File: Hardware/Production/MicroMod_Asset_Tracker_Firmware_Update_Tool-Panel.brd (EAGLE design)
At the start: 199.6 x 83.1 mm, 582 parts, among them J12 MICROMOD-2222, J15 MICROMOD-2222, J18 MICROMOD-2222, J21 MICROMOD-2222, J24 MICROMOD-2222, J27 MICROMOD-2222, J30 MICROMOD-2222, J33 MICROMOD-2222, J36 MICROMOD-2222, J39 MICROMOD-2222, J42 MICROMOD-2222, J45 MICROMOD-2222, J48 MICROMOD-2222, J5 MICROMOD-2222, J6 MICROMOD-2222, J9 MICROMOD-2222, U1 CH340G, U10 CH340G, U11 CH340G, U12 CH340G, U13 CH340G, U14 CH340G, U15 CH340G, U16 CH340G, U2 CH340G, U3 CH340G, U4 CH340G, U5 CH340G, U6 CH340G, U7 CH340G, U8 CH340G, U9 CH340G, Y1 12MHz, Y10 12MHz, Y11 12MHz, Y12 12MHz, Y13 12MHz, Y14 12MHz, Y15 12MHz, Y16 12MHz, Y2 12MHz, Y3 12MHz, Y4 12MHz, Y5 12MHz, Y6 12MHz, Y7 12MHz, Y8 12MHz, Y9 12MHz

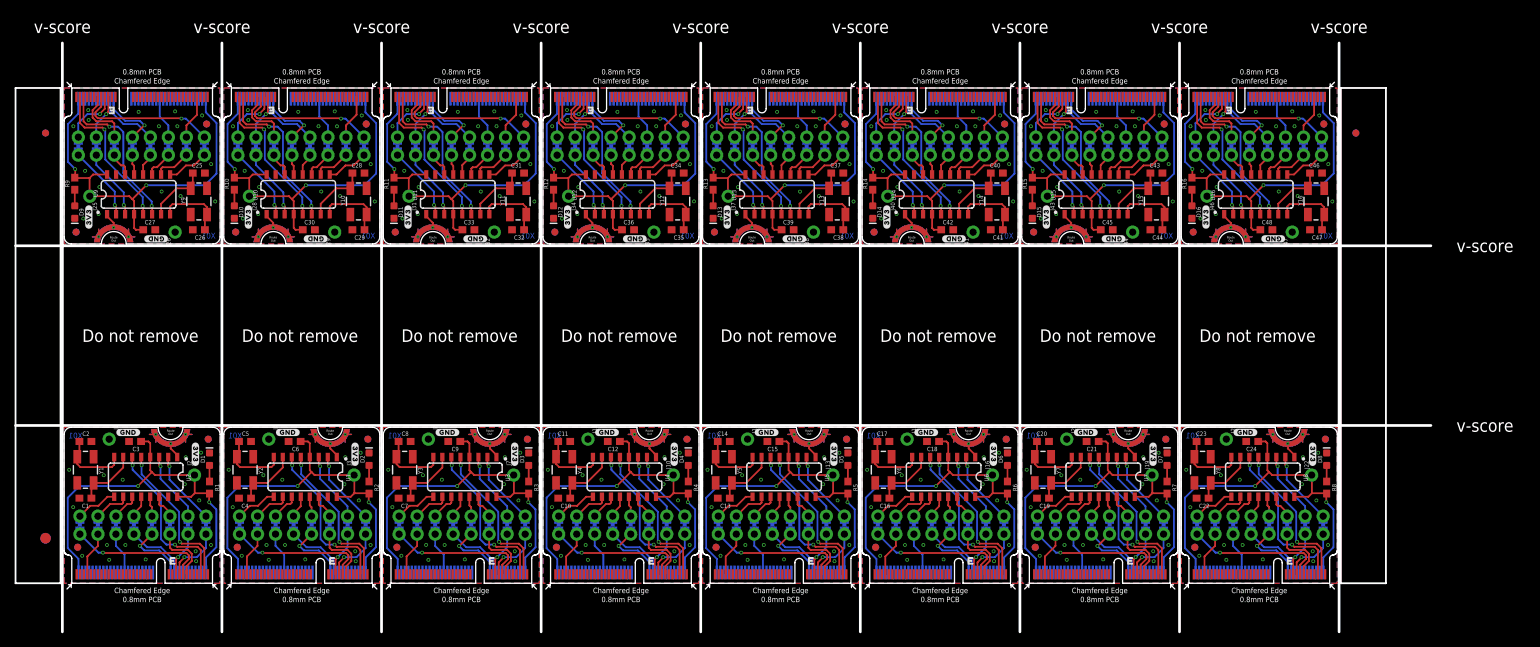
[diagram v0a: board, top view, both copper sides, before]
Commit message: Changed to the CH340C
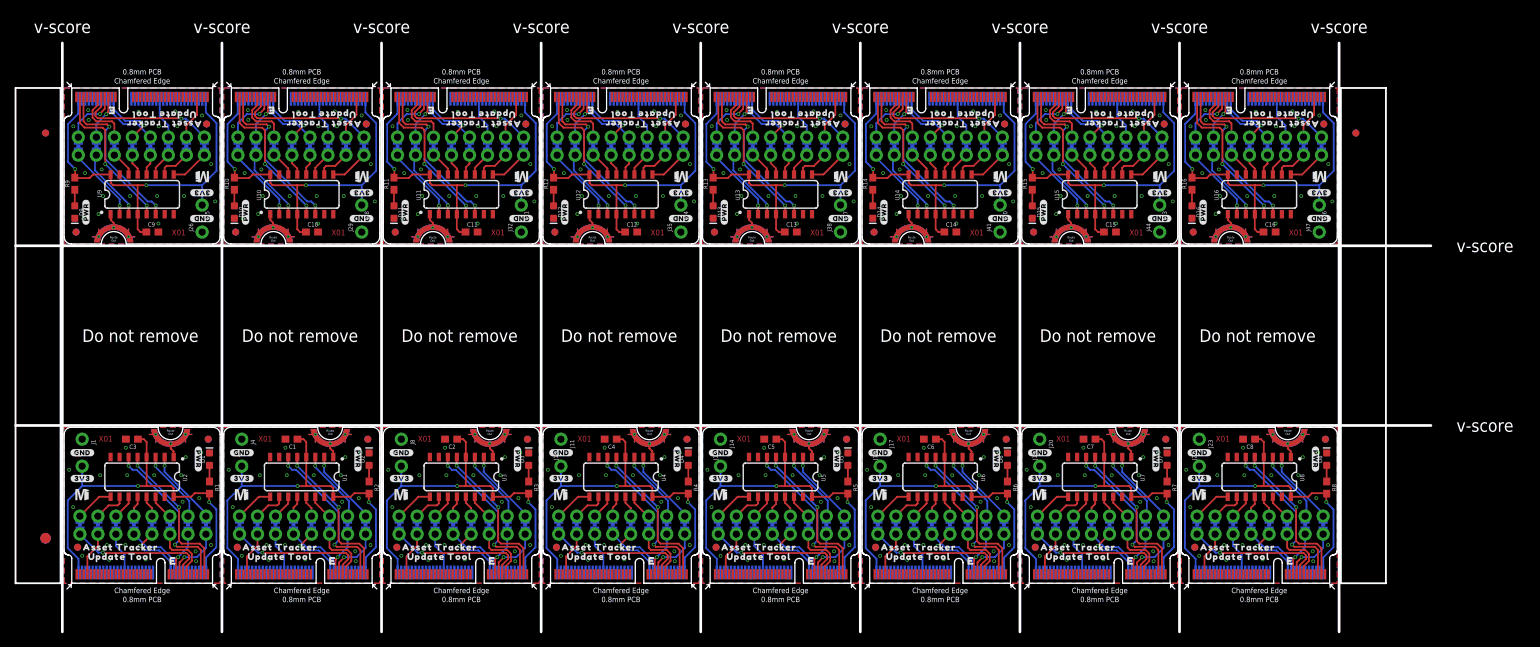
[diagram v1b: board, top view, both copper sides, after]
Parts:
- removed C17, C19, C20, C22, C23, C25, C26, C28, C29, C31, C32, C34, C35, C37, C38, C40, C41, C43, C44, C46, C47: 18pF, SparkFun-Capacitors:0603
- removed C18, C21, C24, C27, C30, C33, C36, C39, C42, C45, C48: 0.1uF, SparkFun-Capacitors:0603
- removed Y1, Y10, Y11, Y12, Y13, Y14, Y15, Y16, Y2, Y3, Y4, Y5, Y6, Y7, Y8, Y9: 12MHz, SparkFun-Clocks:CRYSTAL-SMD-5X3.2-4PAD
- added U$193, U$204, U$209, U$220, U$225, U$236, U$241, U$252: (no value), output:#GND#2
- added U$194, U$203, U$210, U$219, U$226, U$235, U$242, U$251: (no value), output:#3V3#3
- added U$195, U$211, U$227, U$243: (no value), output:#CTS#0
- added U$196, U$212, U$228, U$244: (no value), output:#DSR#0
- added U$197, U$213, U$229, U$245: (no value), output:#RTS#0
- added U$198, U$214, U$230, U$246: (no value), output:#DCD#0
- added U$199, U$215, U$231, U$247: (no value), output:#TX#0
- added U$200, U$216, U$232, U$248: (no value), output:#RX#0
- added U$201, U$217, U$233, U$249: (no value), output:#DTR#0
- added U$202, U$218, U$234, U$250: (no value), output:#RI#0
- added U$205, U$221, U$237, U$253: (no value), output:#PWR#0
- added U$206, U$222, U$238, U$254: (no value), SparkFun-MicroMod:MICROMOD_MI_LOGO_.35
- added U$207, U$223, U$239, U$255: (no value), output:ASSET_TRACKER0
- added U$208, U$224, U$240, U$256: (no value), output:UPDATE_TOOL0
- C1, C10, C11, C13, C14, C16, C2, C4, C5, C7, C8: value 18pF -> 0.1uF
- U$10, U$111, U$159, U$63: device output:#CTS#0 -> output:ASSET_TRACKER0
- U$109, U$157, U$61, U$8: device output:#GND#2 -> output:#PWR#0
- U$11, U$112, U$160, U$64: device output:#DSR#0 -> output:UPDATE_TOOL0
- U$110, U$158, U$62, U$9: device output:#3V3#3 -> SparkFun-MicroMod:MICROMOD_MI_LOGO_.35
- U$113, U$12, U$161, U$65: device output:#RTS#0 -> output:#GND#2
- U$114, U$13, U$162, U$66: device output:#DCD#0 -> output:#3V3#3
- U$115, U$15, U$163, U$67: device output:#TX#0 -> output:#CTS#0
- U$116, U$16, U$164, U$68: device output:#RX#0 -> output:#DSR#0
- U$117, U$165, U$19, U$69: device output:#DTR#0 -> output:#RTS#0
- U$118, U$166, U$21, U$70: device output:#RI#0 -> output:#DCD#0
- U$119, U$167, U$22, U$71: device output:#3V3#3 -> output:#TX#0
- U$120, U$168, U$24, U$72: device output:#GND#2 -> output:#RX#0
- U$121, U$169, U$25, U$73: device output:#GND#2 -> output:#DTR#0
- U$122, U$170, U$26, U$74: device output:#3V3#3 -> output:#RI#0
- U$123, U$171, U$27, U$75: device output:#CTS#0 -> output:#3V3#3
- U$124, U$172, U$28, U$76: device output:#DSR#0 -> output:#GND#2
- U$125, U$173, U$29, U$77: device output:#RTS#0 -> output:#PWR#0
- U$126, U$174, U$30, U$78: device output:#DCD#0 -> SparkFun-MicroMod:MICROMOD_MI_LOGO_.35
- U$127, U$175, U$31, U$79: device output:#TX#0 -> output:ASSET_TRACKER0
- U$128, U$176, U$32, U$80: device output:#RX#0 -> output:UPDATE_TOOL0
- U$129, U$177, U$33, U$81: device output:#DTR#0 -> output:#GND#2
- U$130, U$178, U$34, U$82: device output:#RI#0 -> output:#3V3#3
- U$131, U$179, U$35, U$83: device output:#3V3#3 -> output:#CTS#0
- U$132, U$180, U$36, U$84: device output:#GND#2 -> output:#DSR#0
- U$133, U$181, U$37, U$85: device output:#GND#2 -> output:#RTS#0
- U$134, U$182, U$38, U$86: device output:#3V3#3 -> output:#DCD#0
- U$135, U$183, U$39, U$87: device output:#CTS#0 -> output:#TX#0
- U$136, U$184, U$40, U$88: device output:#DSR#0 -> output:#RX#0
- U$137, U$185, U$41, U$89: device output:#RTS#0 -> output:#DTR#0
- U$138, U$186, U$42, U$90: device output:#DCD#0 -> output:#RI#0
- U$139, U$187, U$43, U$91: device output:#TX#0 -> output:#3V3#3
- U$140, U$188, U$44, U$92: device output:#RX#0 -> output:#GND#2
- U$141, U$189, U$45, U$93: device output:#DTR#0 -> output:#PWR#0
- U$142, U$190, U$46, U$94: device output:#RI#0 -> SparkFun-MicroMod:MICROMOD_MI_LOGO_.35
- U$143, U$191, U$47, U$95: device output:#3V3#3 -> output:ASSET_TRACKER0
- U$144, U$192, U$48, U$96: device output:#GND#2 -> output:UPDATE_TOOL0
- U1, U10, U11, U12, U13, U14, U15, U16, U2, U3, U4, U5, U6, U7, U8, U9: value CH340G -> CH340C
- moved U$103 159.6 mm to (155.1, 12.3), turned to 90 degrees
- moved U$119 156.6 mm to (177.6, 12.3), turned to 90 degrees
- moved U$104 154.8 mm to (152.5, 12.3), turned to 90 degrees
- moved U$101 149.7 mm to (149.9, 12.5), turned to 90 degrees
- moved U$117 147.3 mm to (172.4, 12.5), turned to 90 degrees
- moved U$105 144.9 mm to (147.4, 12.5), turned to 90 degrees
- moved U$120 144.2 mm to (175.0, 12.3), turned to 90 degrees
- moved U$116 142.6 mm to (162.3, 12.4), turned to 90 degrees
- moved U$115 142.6 mm to (159.8, 12.5), turned to 90 degrees
- moved U$102 140.1 mm to (144.9, 12.5), turned to 90 degrees
- moved U$98 139.1 mm to (137.6, 14.8), turned to 0 degrees
- moved U$107 139.1 mm to (137.6, 14.8), turned to 0 degrees
- moved U$118 137.9 mm to (167.4, 12.5), turned to 90 degrees
- moved U$113 136.2 mm to (160.1, 18.4), flipped to the top, turned to 0 degrees
- moved U$106 135.7 mm to (142.4, 11.9), turned to 90 degrees
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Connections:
- removed net N$1 (its old number): C2.2, U2.8, Y1.1
- removed net N$10 (its old number): C10.2, U4.7, Y4.3
- removed net N$11 (its old number): C11.2, U4.8, Y4.1
- removed net N$13 (its old number): C13.2, U5.7, Y5.3
- removed net N$14 (its old number): C14.2, U5.8, Y5.1
- removed net N$16 (its old number): C16.2, U6.7, Y6.3
- removed net N$17: C17.2, U6.8, Y6.1
- removed net N$19: C19.2, U7.7, Y7.3
- removed net N$2 (its old number): C1.2, U2.7, Y1.3
- removed net N$20: C20.2, U7.8, Y7.1
- removed net N$22: C22.2, U8.7, Y8.3
- removed net N$23: C23.2, U8.8, Y8.1
- removed net N$25: C25.2, U9.7, Y9.3
- removed net N$26: C26.2, U9.8, Y9.1
- removed net N$28: C28.2, U10.7, Y10.3
- removed net N$29: C29.2, U10.8, Y10.1
- removed net N$31: C31.2, U11.7, Y11.3
- removed net N$32: C32.2, U11.8, Y11.1
- removed net N$34: C34.2, U12.7, Y12.3
- removed net N$35: C35.2, U12.8, Y12.1
- removed net N$37: C37.2, U13.7, Y13.3
- removed net N$38: C38.2, U13.8, Y13.1
- removed net N$4 (its old number): C4.2, U1.7, Y2.3
- removed net N$40: C40.2, U14.7, Y14.3
- removed net N$41: C41.2, U14.8, Y14.1
- removed net N$43: C43.2, U15.7, Y15.3
- removed net N$44: C44.2, U15.8, Y15.1
- removed net N$46: C46.2, U16.7, Y16.3
- removed net N$47: C47.2, U16.8, Y16.1
- removed net N$5 (its old number): C5.2, U1.8, Y2.1
- removed net N$7 (its old number): C7.2, U3.7, Y3.3
- removed net N$8 (its old number): C8.2, U3.8, Y3.1
- net 3.3V1: now also C1.1; no longer C6.1
- net 3.3V10: now also C11.1; no longer C33.1
- net 3.3V11: now also C12.1; no longer C36.1
- net 3.3V12: now also C13.1; no longer C39.1
- net 3.3V13: now also C14.1; no longer C42.1
- net 3.3V14: now also C15.1; no longer C45.1
- net 3.3V15: now also C16.1; no longer C48.1
- net 3.3V2: now also C2.1; no longer C9.1
- net 3.3V3: now also C4.1; no longer C12.1
- net 3.3V4: now also C5.1; no longer C15.1
- net 3.3V5: now also C6.1; no longer C18.1
- net 3.3V6: now also C7.1; no longer C21.1
- net 3.3V7: now also C8.1; no longer C24.1
- net 3.3V8: now also C9.1; no longer C27.1
- net 3.3V9: now also C10.1; no longer C30.1
- net GND: no longer C1.1, C2.1
- net GND1: now also C1.2; no longer C4.1, C5.1, C6.2
- net GND10: now also C11.2; no longer C31.1, C32.1, C33.2
- net GND11: now also C12.2; no longer C34.1, C35.1, C36.2
- net GND12: now also C13.2; no longer C37.1, C38.1, C39.2
- net GND13: now also C14.2; no longer C40.1, C41.1, C42.2
- net GND14: now also C15.2; no longer C43.1, C44.1, C45.2
- net GND15: now also C16.2; no longer C46.1, C47.1, C48.2
- net GND2: now also C2.2; no longer C7.1, C8.1, C9.2
- net GND3: now also C4.2; no longer C10.1, C11.1, C12.2
- net GND4: now also C5.2; no longer C13.1, C14.1, C15.2
- net GND5: now also C6.2; no longer C16.1, C17.1, C18.2
- net GND6: now also C7.2; no longer C19.1, C20.1, C21.2
- net GND7: now also C8.2; no longer C22.1, C23.1, C24.2
- net GND8: now also C9.2; no longer C25.1, C26.1, C27.2
- net GND9: now also C10.2; no longer C28.1, C29.1, C30.2
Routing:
- net N$47: track 9.92 -> 0.00 mm
- net N$44: track 9.92 -> 0.00 mm
- net N$29: track 9.92 -> 0.00 mm
- net N$26: track 9.92 -> 0.00 mm
- net N$1 (its old number): track 9.92 -> 0.00 mm
- net N$5 (its old number): track 9.92 -> 0.00 mm
- net N$11 (its old number): track 9.92 -> 0.00 mm
- net N$8 (its old number): track 9.92 -> 0.00 mm
- net N$17: track 9.92 -> 0.00 mm
- net N$14 (its old number): track 9.92 -> 0.00 mm
- net N$38: track 9.92 -> 0.00 mm
- net N$35: track 9.92 -> 0.00 mm
- net N$32: track 9.92 -> 0.00 mm
- net N$23: track 9.92 -> 0.00 mm
- net N$20: track 9.92 -> 0.00 mm
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
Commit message: Updates for v10
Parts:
- removed SPARKX1, SPARKX10, SPARKX11, SPARKX12, SPARKX13, SPARKX14, SPARKX15, SPARKX16, SPARKX2, SPARKX3, SPARKX4, SPARKX5, SPARKX6, SPARKX7, SPARKX8, SPARKX9: SPARKX-LOGO4, SparkX:SPARKX-MEDIUM
- added LOGO17, LOGO19, LOGO21, LOGO23, LOGO25, LOGO27, LOGO29, LOGO31: OSHW-LOGOMINI, SparkFun-Aesthetics:OSHW-LOGO-MINI
- added LOGO18, LOGO20, LOGO22, LOGO24, LOGO26, LOGO28, LOGO30, LOGO32: SFE_LOGO_NAME_FLAME.1_INCH, SparkFun-Aesthetics:SFE_LOGO_NAME_FLAME_.1
- added U$257, U$266: (no value), output:#3V3#3
- added U$258: (no value), output:#CTS#0
- added U$259: (no value), output:#DSR#0
- added U$260: (no value), output:#RTS#0
- added U$261: (no value), output:#DCD#0
- added U$262: (no value), output:#TX#0
- added U$263: (no value), output:#RX#0
- added U$264: (no value), output:#DTR#0
- added U$265: (no value), output:#RI#0
- added U$267: (no value), output:#GND#2
- added U$268: (no value), output:#PWR#0
- added U$269: (no value), SparkFun-MicroMod:MICROMOD_MI_LOGO_.35
- added U$270: (no value), output:ASSET_TRACKER0
- added U$271: (no value), output:UPDATE_TOOL0
- added U$272: (no value), SparkFun-MicroMod:MICROMOD_LOGO_.35
- LOGO10, LOGO12, LOGO14, LOGO16, LOGO3, LOGO4, LOGO6, LOGO8: value OSHW-LOGOMINI -> SFE_LOGO_NAME_FLAME.1_INCH; device SparkFun-Aesthetics:OSHW-LOGO-MINI -> SparkFun-Aesthetics:SFE_LOGO_NAME_FLAME_.1
- U$100: device output:#DSR#0 -> output:ASSET_TRACKER0
- U$101: device output:#RTS#0 -> output:UPDATE_TOOL0
- U$102: device output:#DCD#0 -> SparkFun-MicroMod:MICROMOD_LOGO_.35
- U$103, U$199: device output:#TX#0 -> output:#GND#2
- U$104, U$232: device output:#RX#0 -> output:#3V3#3
- U$105: device output:#DTR#0 -> output:#CTS#0
- U$106: device output:#RI#0 -> output:#DSR#0
- U$107, U$226: device output:#3V3#3 -> output:#RTS#0
- U$108, U$193: device output:#GND#2 -> output:#DCD#0
- U$109: device output:#PWR#0 -> output:#TX#0
- U$110: device SparkFun-MicroMod:MICROMOD_MI_LOGO_.35 -> output:#RX#0
- U$111: device output:ASSET_TRACKER0 -> output:#DTR#0
- U$112: device output:UPDATE_TOOL0 -> output:#RI#0
- U$113, U$172, U$28: device output:#GND#2 -> output:#3V3#3
- U$114, U$13, U$171: device output:#3V3#3 -> output:#GND#2
- U$115: device output:#CTS#0 -> output:#PWR#0
- U$116: device output:#DSR#0 -> SparkFun-MicroMod:MICROMOD_MI_LOGO_.35
- U$117: device output:#RTS#0 -> output:ASSET_TRACKER0
- U$118: device output:#DCD#0 -> output:UPDATE_TOOL0
- U$119: device output:#TX#0 -> SparkFun-MicroMod:MICROMOD_LOGO_.35
- U$12, U$204: device output:#GND#2 -> SparkFun-MicroMod:MICROMOD_LOGO_.35
- U$120, U$216: device output:#RX#0 -> output:#GND#2
- U$121, U$249: device output:#DTR#0 -> output:#3V3#3
- U$122: device output:#RI#0 -> output:#CTS#0
- U$123, U$242: device output:#3V3#3 -> output:#DSR#0
- U$124, U$209: device output:#GND#2 -> output:#RTS#0
- U$125: device output:#PWR#0 -> output:#DCD#0
- U$126: device SparkFun-MicroMod:MICROMOD_MI_LOGO_.35 -> output:#TX#0
- U$127: device output:ASSET_TRACKER0 -> output:#RX#0
- U$128: device output:UPDATE_TOOL0 -> output:#DTR#0
- U$129, U$44: device output:#GND#2 -> output:#RI#0
- U$131, U$35: device output:#CTS#0 -> output:#GND#2
- U$132: device output:#DSR#0 -> output:#PWR#0
- U$133: device output:#RTS#0 -> SparkFun-MicroMod:MICROMOD_MI_LOGO_.35
- U$134: device output:#DCD#0 -> output:ASSET_TRACKER0
- U$135: device output:#TX#0 -> output:UPDATE_TOOL0
- U$136: device output:#RX#0 -> SparkFun-MicroMod:MICROMOD_LOGO_.35
- U$137, U$233: device output:#DTR#0 -> output:#GND#2
- U$138: device output:#RI#0 -> output:#3V3#3
- U$139: device output:#3V3#3 -> output:#CTS#0
- U$140, U$225: device output:#GND#2 -> output:#DSR#0
- U$141: device output:#PWR#0 -> output:#RTS#0
- U$142: device SparkFun-MicroMod:MICROMOD_MI_LOGO_.35 -> output:#DCD#0
- U$143: device output:ASSET_TRACKER0 -> output:#TX#0
- U$144: device output:UPDATE_TOOL0 -> output:#RX#0
- U$145, U$60: device output:#GND#2 -> output:#DTR#0
- U$146, U$27: device output:#3V3#3 -> output:#RI#0
- U$147, U$15: device output:#CTS#0 -> output:#3V3#3
- U$148, U$52: device output:#DSR#0 -> output:#GND#2
- U$149: device output:#RTS#0 -> output:#PWR#0
- U$150: device output:#DCD#0 -> SparkFun-MicroMod:MICROMOD_MI_LOGO_.35
- U$151: device output:#TX#0 -> output:ASSET_TRACKER0
- U$152: device output:#RX#0 -> output:UPDATE_TOOL0
- U$153: device output:#DTR#0 -> SparkFun-MicroMod:MICROMOD_LOGO_.35
- U$154, U$250: device output:#RI#0 -> output:#GND#2
- U$156, U$241: device output:#GND#2 -> output:#CTS#0
- U$157: device output:#PWR#0 -> output:#DSR#0
- U$158: device SparkFun-MicroMod:MICROMOD_MI_LOGO_.35 -> output:#RTS#0
- U$159: device output:ASSET_TRACKER0 -> output:#DCD#0
- U$16: device output:#DSR#0 -> output:#CTS#0
- U$160: device output:UPDATE_TOOL0 -> output:#TX#0
- U$161, U$76: device output:#GND#2 -> output:#RX#0
- U$162, U$43: device output:#3V3#3 -> output:#DTR#0
- U$163: device output:#CTS#0 -> output:#RI#0
- U$164, U$36: device output:#DSR#0 -> output:#3V3#3
- U$165, U$69: device output:#RTS#0 -> output:#GND#2
- U$166: device output:#DCD#0 -> output:#PWR#0
- U$167: device output:#TX#0 -> SparkFun-MicroMod:MICROMOD_MI_LOGO_.35
- U$168: device output:#RX#0 -> output:ASSET_TRACKER0
- U$169: device output:#DTR#0 -> output:UPDATE_TOOL0
- U$170: device output:#RI#0 -> SparkFun-MicroMod:MICROMOD_LOGO_.35
- U$173: device output:#PWR#0 -> output:#CTS#0
- U$174: device SparkFun-MicroMod:MICROMOD_MI_LOGO_.35 -> output:#DSR#0
- U$175: device output:ASSET_TRACKER0 -> output:#RTS#0
- U$176: device output:UPDATE_TOOL0 -> output:#DCD#0
- U$177, U$92: device output:#GND#2 -> output:#TX#0
- U$178, U$59: device output:#3V3#3 -> output:#RX#0
- U$179: device output:#CTS#0 -> output:#DTR#0
- U$180: device output:#DSR#0 -> output:#RI#0
- U$181, U$53: device output:#RTS#0 -> output:#3V3#3
- U$182, U$86: device output:#DCD#0 -> output:#GND#2
- U$183: device output:#TX#0 -> output:#PWR#0
- U$184: device output:#RX#0 -> SparkFun-MicroMod:MICROMOD_MI_LOGO_.35
- U$185: device output:#DTR#0 -> output:ASSET_TRACKER0
- U$186: device output:#RI#0 -> output:UPDATE_TOOL0
- U$187, U$34: device output:#3V3#3 -> SparkFun-MicroMod:MICROMOD_LOGO_.35
- U$189, U$45: device output:#PWR#0 -> output:#3V3#3
- U$19: device output:#RTS#0 -> output:#DSR#0
- U$190: device SparkFun-MicroMod:MICROMOD_MI_LOGO_.35 -> output:#CTS#0
- U$191: device output:ASSET_TRACKER0 -> output:#DSR#0
- U$192: device output:UPDATE_TOOL0 -> output:#RTS#0
- U$194, U$75: device output:#3V3#3 -> output:#TX#0
- U$195: device output:#CTS#0 -> output:#RX#0
- U$196: device output:#DSR#0 -> output:#DTR#0
- U$197: device output:#RTS#0 -> output:#RI#0
- U$198, U$70: device output:#DCD#0 -> output:#3V3#3
- U$200: device output:#RX#0 -> output:#PWR#0
- U$201: device output:#DTR#0 -> SparkFun-MicroMod:MICROMOD_MI_LOGO_.35
- U$202: device output:#RI#0 -> output:ASSET_TRACKER0
- U$203, U$50: device output:#3V3#3 -> output:UPDATE_TOOL0
- U$205, U$29: device output:#PWR#0 -> output:#GND#2
- U$206, U$62: device SparkFun-MicroMod:MICROMOD_MI_LOGO_.35 -> output:#3V3#3
- U$207: device output:ASSET_TRACKER0 -> output:#CTS#0
- U$208: device output:UPDATE_TOOL0 -> output:#DSR#0
- U$21: device output:#DCD#0 -> output:#RTS#0
- U$210, U$91: device output:#3V3#3 -> output:#DCD#0
- U$211: device output:#CTS#0 -> output:#TX#0
- U$212: device output:#DSR#0 -> output:#RX#0
- U$213: device output:#RTS#0 -> output:#DTR#0
- U$214: device output:#DCD#0 -> output:#RI#0
- U$215, U$87: device output:#TX#0 -> output:#3V3#3
- U$217: device output:#DTR#0 -> output:#PWR#0
- U$218: device output:#RI#0 -> SparkFun-MicroMod:MICROMOD_MI_LOGO_.35
- U$219, U$66: device output:#3V3#3 -> output:ASSET_TRACKER0
- U$22: device output:#TX#0 -> output:#DCD#0
- U$220, U$33: device output:#GND#2 -> output:UPDATE_TOOL0
- U$221: device output:#PWR#0 -> SparkFun-MicroMod:MICROMOD_LOGO_.35
- U$222, U$46: device SparkFun-MicroMod:MICROMOD_MI_LOGO_.35 -> output:#GND#2
- U$223, U$79: device output:ASSET_TRACKER0 -> output:#3V3#3
- U$224: device output:UPDATE_TOOL0 -> output:#CTS#0
- U$227: device output:#CTS#0 -> output:#DCD#0
- U$228: device output:#DSR#0 -> output:#TX#0
- U$229: device output:#RTS#0 -> output:#RX#0
- U$230: device output:#DCD#0 -> output:#DTR#0
- U$231: device output:#TX#0 -> output:#RI#0
- U$234: device output:#RI#0 -> output:#PWR#0
- U$235, U$82: device output:#3V3#3 -> SparkFun-MicroMod:MICROMOD_MI_LOGO_.35
- U$236, U$49: device output:#GND#2 -> output:ASSET_TRACKER0
- U$237: device output:#PWR#0 -> output:UPDATE_TOOL0
- U$238: device SparkFun-MicroMod:MICROMOD_MI_LOGO_.35 -> SparkFun-MicroMod:MICROMOD_LOGO_.35
- U$239, U$63: device output:ASSET_TRACKER0 -> output:#GND#2
- U$24: device output:#RX#0 -> output:#TX#0
- U$240, U$96: device output:UPDATE_TOOL0 -> output:#3V3#3
- U$243: device output:#CTS#0 -> output:#RTS#0
- U$244: device output:#DSR#0 -> output:#DCD#0
- U$245: device output:#RTS#0 -> output:#TX#0
- U$246: device output:#DCD#0 -> output:#RX#0
- U$247: device output:#TX#0 -> output:#DTR#0
- U$248: device output:#RX#0 -> output:#RI#0
- U$25: device output:#DTR#0 -> output:#RX#0
- U$251, U$98: device output:#3V3#3 -> output:#PWR#0
- U$252, U$65: device output:#GND#2 -> SparkFun-MicroMod:MICROMOD_MI_LOGO_.35
- U$253: device output:#PWR#0 -> output:ASSET_TRACKER0
- U$254: device SparkFun-MicroMod:MICROMOD_MI_LOGO_.35 -> output:UPDATE_TOOL0
- U$255: device output:ASSET_TRACKER0 -> SparkFun-MicroMod:MICROMOD_LOGO_.35
- U$256, U$80: device output:UPDATE_TOOL0 -> output:#GND#2
- U$26: device output:#RI#0 -> output:#DTR#0
- U$30: device SparkFun-MicroMod:MICROMOD_MI_LOGO_.35 -> output:#PWR#0
- U$31: device output:ASSET_TRACKER0 -> SparkFun-MicroMod:MICROMOD_MI_LOGO_.35
- U$32: device output:UPDATE_TOOL0 -> output:ASSET_TRACKER0
- U$37: device output:#RTS#0 -> output:#CTS#0
- U$38: device output:#DCD#0 -> output:#DSR#0
- U$39: device output:#TX#0 -> output:#RTS#0
- U$40: device output:#RX#0 -> output:#DCD#0
- U$41: device output:#DTR#0 -> output:#TX#0
- U$42: device output:#RI#0 -> output:#RX#0
- U$47: device output:ASSET_TRACKER0 -> output:#PWR#0
- U$48: device output:UPDATE_TOOL0 -> SparkFun-MicroMod:MICROMOD_MI_LOGO_.35
- U$51: device output:#CTS#0 -> SparkFun-MicroMod:MICROMOD_LOGO_.35
- U$54: device output:#DCD#0 -> output:#CTS#0
- U$55: device output:#TX#0 -> output:#DSR#0
- U$56: device output:#RX#0 -> output:#RTS#0
- U$57: device output:#DTR#0 -> output:#DCD#0
- U$58: device output:#RI#0 -> output:#TX#0
- U$61: device output:#PWR#0 -> output:#RI#0
- U$64: device output:UPDATE_TOOL0 -> output:#PWR#0
- U$67: device output:#CTS#0 -> output:UPDATE_TOOL0
- U$68: device output:#DSR#0 -> SparkFun-MicroMod:MICROMOD_LOGO_.35
- U$71: device output:#TX#0 -> output:#CTS#0
- U$72: device output:#RX#0 -> output:#DSR#0
- U$73: device output:#DTR#0 -> output:#RTS#0
- U$74: device output:#RI#0 -> output:#DCD#0
- U$77: device output:#PWR#0 -> output:#DTR#0
- U$78: device SparkFun-MicroMod:MICROMOD_MI_LOGO_.35 -> output:#RI#0
- U$81: device output:#GND#2 -> output:#PWR#0
- U$83: device output:#CTS#0 -> output:ASSET_TRACKER0
- U$84: device output:#DSR#0 -> output:UPDATE_TOOL0
- U$85: device output:#RTS#0 -> SparkFun-MicroMod:MICROMOD_LOGO_.35
- U$88: device output:#RX#0 -> output:#CTS#0
- U$89: device output:#DTR#0 -> output:#DSR#0
- U$90: device output:#RI#0 -> output:#RTS#0
- U$93: device output:#PWR#0 -> output:#RX#0
- U$94: device SparkFun-MicroMod:MICROMOD_MI_LOGO_.35 -> output:#DTR#0
- U$95: device output:ASSET_TRACKER0 -> output:#RI#0
- U$99: device output:#CTS#0 -> SparkFun-MicroMod:MICROMOD_MI_LOGO_.35
- moved U$135 172.1 mm to (165.5, 3.75), flipped to the top, turned to 0 degrees
- moved U$136 168.5 mm to (167.8, 15.9), turned to 0 degrees
- moved U$132 164.2 mm to (176.5, 17.5), flipped to the top
- moved U$134 162.0 mm to (165.5, 5.08), flipped to the top, turned to 0 degrees
- moved U$133 159.4 mm to (160.0, 12.5), flipped to the top, turned to 0 degrees
- moved U$129 150.7 mm to (164.9, 11.9), flipped to the bottom, turned to 90 degrees
- moved U$130 146.4 mm to (160.1, 14.8), flipped to the bottom, turned to 0 degrees
- moved U$131 145.7 mm to (160.1, 18.4), turned to 0 degrees
- moved LOGO9 104.3 mm to (109.9, 17.8), turned to 0 degrees
- moved LOGO8 89.8 mm to (78.8, 17.8)
- moved LOGO11 83.2 mm to (132.4, 17.8), turned to 0 degrees
- moved LOGO10 75.4 mm to (101.3, 17.8), turned to 0 degrees
- moved LOGO6 67.3 mm to (56.3, 17.8)
- moved LOGO13 63.2 mm to (154.9, 17.8), turned to 0 degrees
- moved LOGO7 58.6 mm to (87.4, 17.8)
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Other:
- board text added: "v10"
- board text removed: "X01"
